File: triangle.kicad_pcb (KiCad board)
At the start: 2 copper layers, 80.6 x 72.4 mm, 55 parts, among them J1 Conn_01x02, SW1 SW_SPST

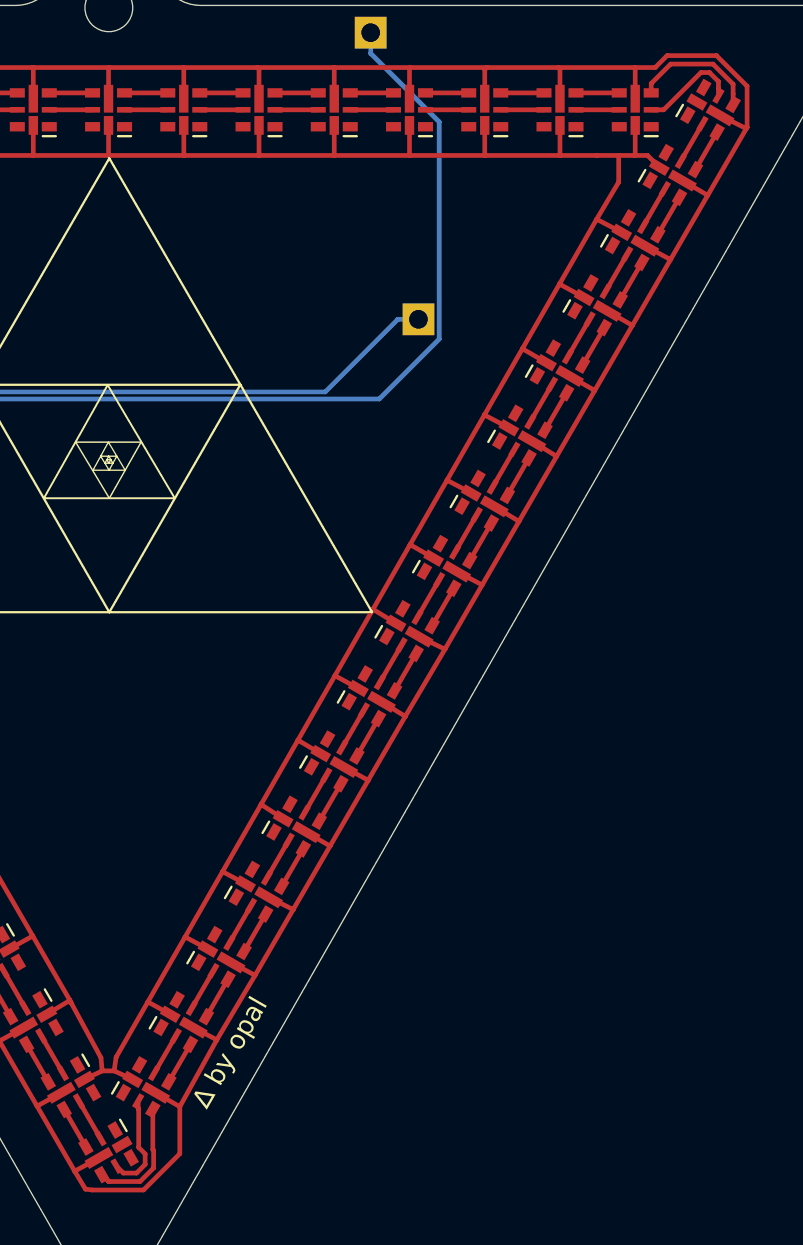
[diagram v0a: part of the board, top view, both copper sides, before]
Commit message: commit the fucking 5v lines to the corner leds...
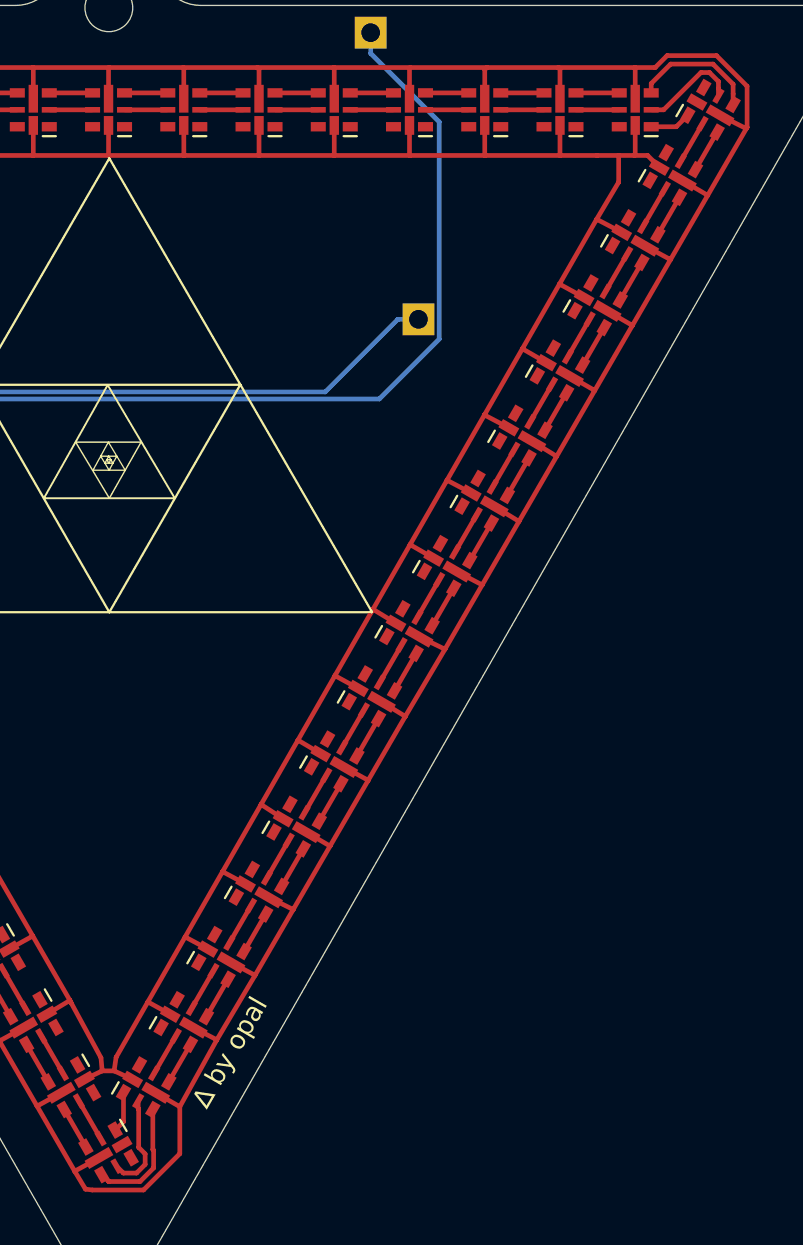
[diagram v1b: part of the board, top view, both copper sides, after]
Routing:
- net +5V: track 271.6 -> 276.0 mm
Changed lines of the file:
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@@
     (thickness 1.6)
     (drawings 42)
-    (tracks 416)
+    (tracks 420)
     (zones 0)
     (modules 55)
@@
   (segment (start 71.8566 63.8937) (end 60.3889 52.426) (width 0.25) (layer B.Cu) (net 99))
   (segment (start 54 52.426) (end 59.3348 52.426) (width 0.25) (layer B.Cu) (net 99))
+  (segment (start 112.181699 50.9) (end 112.795577 50.286122) (width 0.25) (layer F.Cu) (net 99))
+  (segment (start 110.85 50.9) (end 112.181699 50.9) (width 0.25) (layer F.Cu) (net 99))
+  (segment (start 82.795577 103.798349) (end 82.354423 104.239503) (width 0.25) (layer F.Cu) (net 99))
+  (segment (start 82.795577 102.247646) (end 82.795577 103.798349) (width 0.25) (layer F.Cu) (net 99))
   (segment (start 54.5952 48.9976) (end 54.5952 48.5976) (width 0.25) (layer B.Cu) (net 100))
   (segment (start 110 49.41) (end 110 49.409998) (width 0.25) (layer F.Cu) (net 100))

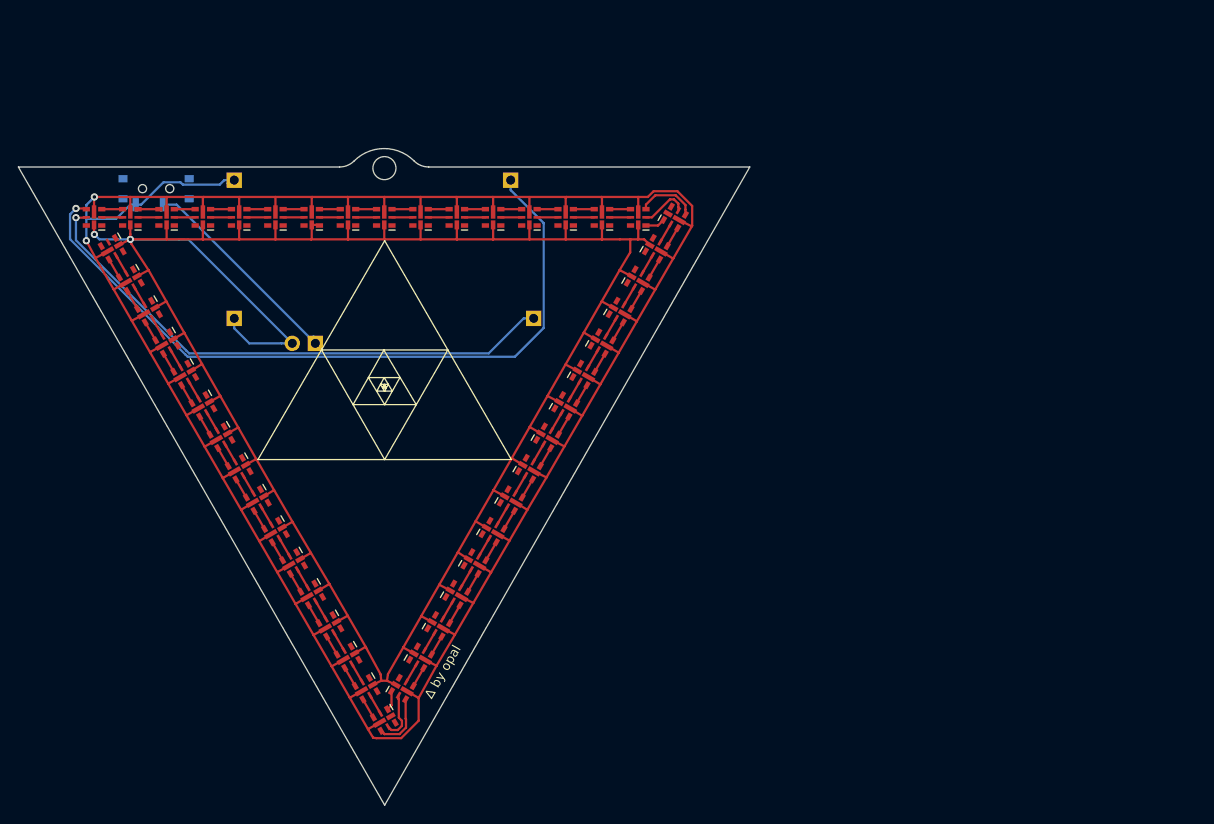
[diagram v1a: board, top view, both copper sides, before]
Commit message: (committing old change) tighten APA102-2020 pad spacing to make it easier (read: possible) to solder
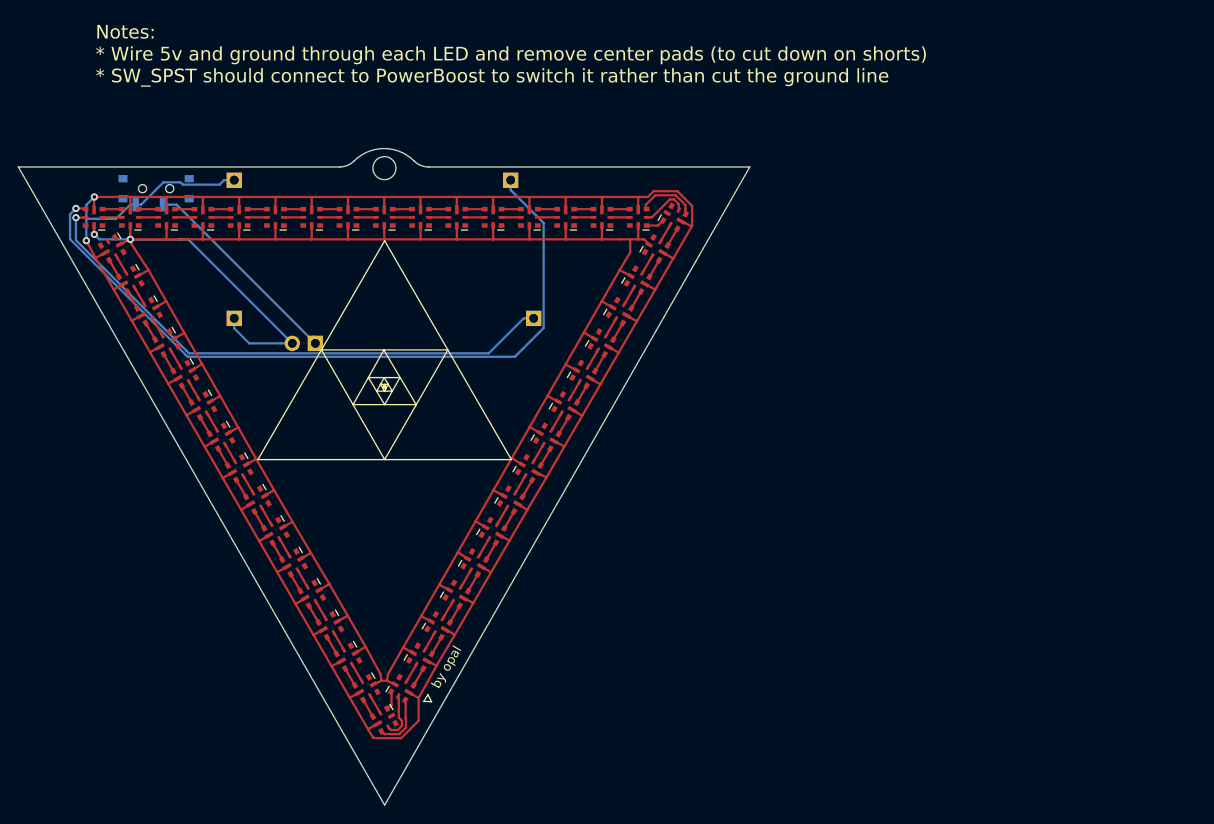
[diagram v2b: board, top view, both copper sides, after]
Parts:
- D0, D1, D10, D11, D12, D13, D14, D15, D16, D17, D18, D19, D2, D20, D21, D22, D23, D24, D25, D26, D27, D28, D29, D3, D30, D31, D32, D33, D34, D35, D36, D37, D38, D39, D4, D40, D41, D42, D43, D44, D45, D46, D47, D5, D6, D7, D8, D9: footprint LED_SMD:LED-APA102-2020 -> LED_SMD:LED-APA102-2020_tightened_pads
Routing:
- net +5V: track 276.0 -> 275.5 mm
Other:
- board text added: "Notes: * Wire 5v and ground through each LED and remove center pads (to cut down on shorts) * SW_SPST should connect to PowerBoost to switch it rather than cut the ground line"
- board text added: "by opal"
- board text removed: "∆ by opal"

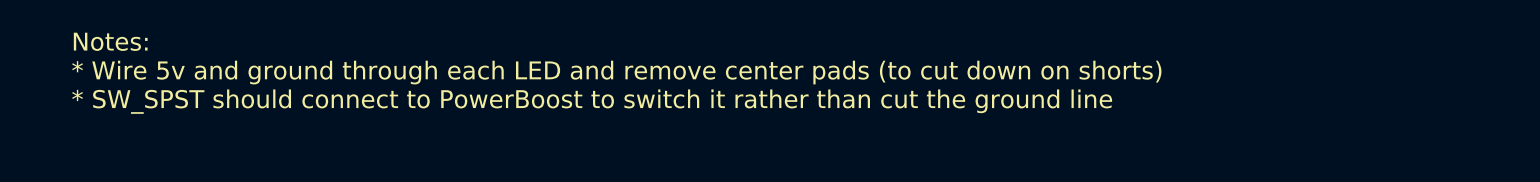
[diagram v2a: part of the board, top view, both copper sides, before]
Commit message: rework/cleanup to make triangle pendant more of a pride-pink-triangle wearable
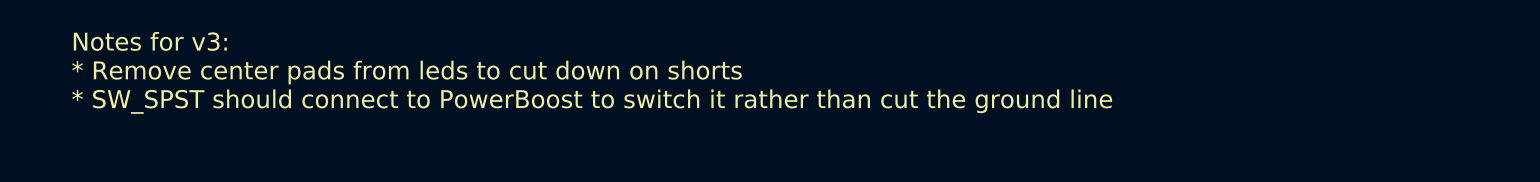
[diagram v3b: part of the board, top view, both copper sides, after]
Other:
- board text added: "Notes for v3: * Remove center pads from leds to cut down on shorts * SW_SPST should connect to PowerBoost to switch it rather than cut the ground line"
- board text removed: "Notes: * Wire 5v and ground through each LED and remove center pads (to cut down on shorts) * SW_SPST should connect to PowerBoost to switch it rather than cut the ground line"
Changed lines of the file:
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@@
-(kicad_pcb (version 20171130) (host pcbnew "(5.1.2-1)-1")
+(kicad_pcb (version 20171130) (host pcbnew "(5.1.5-0-10_14)")
   (general
     (thickness 1.6)
@@
     )
   )
-  (gr_text "Notes:\n* Wire 5v and ground through each LED and remove center pads (to cut down on shorts)\n* SW_SPST should connect to PowerBoost to switch it rather than cut the ground line" (at 50.165 32.004) (layer F.SilkS)
+  (gr_text "Notes for v3:\n* Remove center pads from leds to cut down on shorts\n* SW_SPST should connect to PowerBoost to switch it rather than cut the ground line" (at 50.165 32.004) (layer F.SilkS)
     (effects (font (size 1.5 1.5) (thickness 0.3)) (justify left))
   )
